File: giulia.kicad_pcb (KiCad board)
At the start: 2 copper layers, 129 parts, among them J1 AVR-ISP-6, J2 0548190519, SW1 RESET, SW2 BOOT, U1 ATmega32A-PU, Y1 16 MHz

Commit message: basic component layout
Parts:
- moved SW2 133.4 mm to (199.3, 25.8)
- moved SW1 128.5 mm to (185.2, 22.0)
- moved J1 103.9 mm to (167.1, 28.7), turned to 270 degrees
- moved C3 85.1 mm to (150.5, 53.6)
- moved C2 84.8 mm to (155.6, 31.5), turned to 180 degrees
- moved C5 72.8 mm to (150.6, 22.7)
- moved OL1 72.8 mm to (44.5, 24.0)
- moved Y1 68.2 mm to (146.3, 29.6), turned to 90 degrees
- moved J2 65.9 mm to (136.5, 30.1), turned to 270 degrees
- moved C4 65.7 mm to (150.6, 26.9)
- moved C1 62.3 mm to (125.2, 16.8), turned to 270 degrees
- moved D25 61.4 mm to (185.4, 37.0)
- moved D26 61.0 mm to (189.2, 39.5)
- moved D27 61.0 mm to (193.0, 42.0)
- moved D48 53.3 mm to (113.3, 23.2)
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
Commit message: Adjusting physical component layout
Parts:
- moved C1 15.8 mm to (117.2, 30.4)
- moved SW1 13.4 mm to (172.1, 25.0)
- moved SW2 8.69 mm to (191.4, 29.5), turned to 180 degrees
- moved J1 5.26 mm to (161.9, 29.5), turned to 90 degrees
- moved R1 3.70 mm to (98.0, 23.1)
- moved R2 3.70 mm to (98.0, 26.4)
- moved R4 3.70 mm to (98.0, 33.0)
- moved R3 3.70 mm to (98.0, 29.7)
- moved J2 2.41 mm to (136.5, 27.7)
- moved F1 2.41 mm to (127.8, 29.8)
- moved D49 1.91 mm to (113.3, 26.4)
- moved D29 0.52 mm to (200.2, 39.4)
- moved D30 0.52 mm to (204.0, 41.9)
- moved D32 0.52 mm to (211.6, 36.8)
- moved D33 0.52 mm to (215.4, 39.4)
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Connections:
- SW2 pad 1: Net-(SW2-Pad1) -> BOOT
- U1 pad 18: Net-(SW2-Pad1) -> Net-(U1-Pad18)
- U1 pad 5: Net-(U1-Pad5) -> BOOT
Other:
- board outline added: 240.9 x 112.5 mm
- board text added: "5V"
- board text added: "GND"
- board text added: "MISO"
- board text added: "MOSI"
- board text added: "RST"
- board text added: "SCK"

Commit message: PCB progress
finally placed RGB footprints, added own footprint lib for easy silkscreen adjustment etc.
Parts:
- D1, D10, D11, D12, D13, D14, D15, D16, D17, D18, D19, D2, D20, D21, D22, D23, D24, D25, D26, D27, D28, D29, D3, D30, D31, D32, D33, D34, D35, D36, D37, D38, D39, D4, D40, D41, D42, D43, D44, D45, D46, D47, D5, D6, D7, D8, D9: footprint Diode_THT:D_DO-35_SOD27_P7.62mm_Horizontal -> giulia:D_DO-35_SOD27_P7.62mm_Horizontal_Giulia
- moved D50 367.6 mm to (38.2, 31.5)
- moved D51 314.4 mm to (83.9, 31.5), turned to 180 degrees
- moved D63 289.9 mm to (50.8, 128.9)
- moved D64 283.9 mm to (33.9, 103.8), turned to 270 degrees
- moved D62 267.2 mm to (86.4, 128.9)
- moved D65 264.1 mm to (33.9, 75.7), turned to 270 degrees
- moved D61 250.9 mm to (114.9, 128.9)
- moved D52 241.1 mm to (153.0, 40.0), turned to 180 degrees
- moved D60 229.9 mm to (150.7, 128.9)
- moved D59 210.5 mm to (186.7, 128.9)
- moved D58 189.4 mm to (229.2, 128.9)
- moved D57 182.5 mm to (250.8, 128.9)
- moved D53 169.0 mm to (217.8, 31.5), turned to 180 degrees
- moved D56 147.1 mm to (267.3, 92.5), turned to 90 degrees
- moved D55 128.8 mm to (265.9, 60.3), turned to 90 degrees
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
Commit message: cleaned up libs, removed submodules
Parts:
- OL1: value OLED 128x32 -> OLED; footprint Connector_PinHeader_2.54mm:PinHeader_1x04_P2.54mm_Vertical -> giulia:OLED
- moved OL1 3.68 mm to (44.5, 27.7), turned to 270 degrees

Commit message: the madness that is trace routing begins
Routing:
- net ROW0: track 0.00 -> 237.9 mm, vias 0 -> 1
- net ROW1: track 0.00 -> 233.1 mm, vias 0 -> 1
- net ROW3: track 0.00 -> 232.7 mm
- net ROW2: track 0.00 -> 231.6 mm, vias 0 -> 1
- net +5V: track 0.00 -> 164.4 mm, vias 0 -> 1
- net GND: track 0.00 -> 128.6 mm
- net Net-(D50-Pad4): track 0.00 -> 58.1 mm
- net D+: track 0.00 -> 44.6 mm
- net D-: track 0.00 -> 41.6 mm
- net Net-(D48-Pad1): track 0.00 -> 40.2 mm
- net Net-(D49-Pad1): track 0.00 -> 31.1 mm
- net BOOT: track 0.00 -> 26.7 mm
- net RST: track 0.00 -> 24.1 mm
- net RGB: track 0.00 -> 21.5 mm
- net Net-(C5-Pad1): track 0.00 -> 16.6 mm
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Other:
- net class Default: trace_width 0.25 -> 0.254
- net class Power added: clearance 0.2, trace_width 0.381, via_dia 0.8, via_drill 0.4

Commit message: top layout that makes more sense
imagine that, not using 20 vias for basic USB wiring
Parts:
- moved J2 41.9 mm to (94.6, 27.7)
- moved R2 33.7 mm to (131.7, 25.7), turned to 180 degrees
- moved R3 33.7 mm to (131.7, 29.0), turned to 180 degrees
- moved F1 29.8 mm to (98.2, 33.4), turned to 180 degrees
- moved R1 23.5 mm to (121.5, 22.4)
- moved R4 23.5 mm to (121.5, 32.3)
- moved D58 14.0 mm to (215.3, 128.9)
- moved D48 12.2 mm to (101.6, 26.5)
- moved D49 12.1 mm to (101.6, 23.2)
- moved C1 8.56 mm to (109.2, 33.4), turned to 90 degrees
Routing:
- net COL0: track 0.00 -> 160.4 mm
- net COL1: track 0.00 -> 146.9 mm
- net COL11: track 0.00 -> 137.7 mm
- net COL2: track 0.00 -> 130.4 mm
- net COL10: track 0.00 -> 118.4 mm
- net COL3: track 0.00 -> 113.9 mm
- net COL4: track 0.00 -> 109.8 mm
- net COL9: track 0.00 -> 101.9 mm
- net COL5: track 0.00 -> 92.7 mm
- net COL8: track 0.00 -> 85.4 mm
- net +5V: track 164.4 -> 83.9 mm, vias 1 -> 0
- net COL7: track 0.00 -> 71.2 mm
- net Net-(D50-Pad4): track 58.1 -> 0.00 mm
- net COL6: track 0.00 -> 56.1 mm
- net RST: track 24.1 -> 68.0 mm
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
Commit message: routing progress, diode placement change
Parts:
- moved D16 11.5 mm to (78.7, 38.0)
- moved D24 11.5 mm to (109.2, 38.0)
- moved D8 11.5 mm to (48.3, 38.0)
- moved D13 11.4 mm to (90.2, 44.1)
- moved D21 11.4 mm to (120.7, 44.1)
- moved D5 11.4 mm to (59.7, 44.1)
- moved D15 3.84 mm to (82.5, 40.0)
- moved D23 3.84 mm to (113.0, 40.0)
- moved D7 3.84 mm to (52.1, 40.0)
- moved D14 3.81 mm to (86.4, 42.0)
- moved D22 3.81 mm to (116.8, 42.0)
- moved D6 3.81 mm to (55.9, 42.0)
- moved D12 1.02 mm to (74.9, 38.0)
- moved D20 1.02 mm to (105.4, 38.0)
- moved D4 1.02 mm to (44.5, 38.0)
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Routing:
- net ROW3: track 232.7 -> 119.4 mm
- net ROW2: track 231.6 -> 123.2 mm, vias 1 -> 0
- net ROW0: track 237.9 -> 130.8 mm, vias 1 -> 0
- net ROW1: track 233.1 -> 127.0 mm, vias 1 -> 0
- net Net-(D20-Pad2): track 0.00 -> 95.5 mm
- net Net-(D24-Pad2): track 0.00 -> 94.0 mm
- net Net-(D12-Pad2): track 0.00 -> 90.4 mm
- net Net-(D4-Pad2): track 0.00 -> 81.4 mm
- net Net-(D16-Pad2): track 0.00 -> 81.3 mm
- net Net-(D8-Pad2): track 0.00 -> 78.9 mm
- net Net-(D19-Pad2): track 0.00 -> 77.2 mm
- net Net-(D23-Pad2): track 0.00 -> 68.6 mm
- net Net-(D15-Pad2): track 0.00 -> 62.9 mm
- net Net-(D11-Pad2): track 0.00 -> 62.7 mm
- net Net-(D7-Pad2): track 0.00 -> 61.0 mm
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
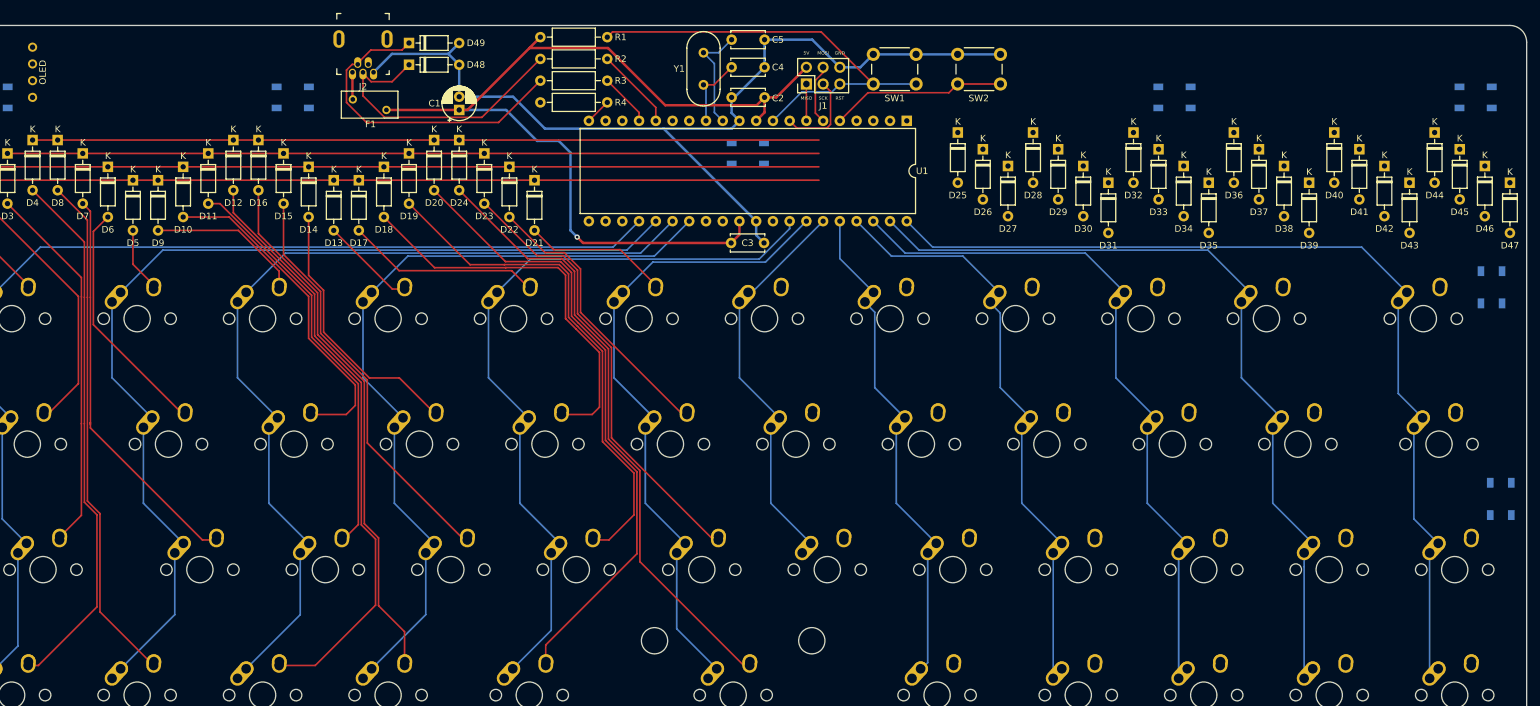
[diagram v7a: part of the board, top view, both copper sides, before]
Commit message: switch routing done, fixed MCU position
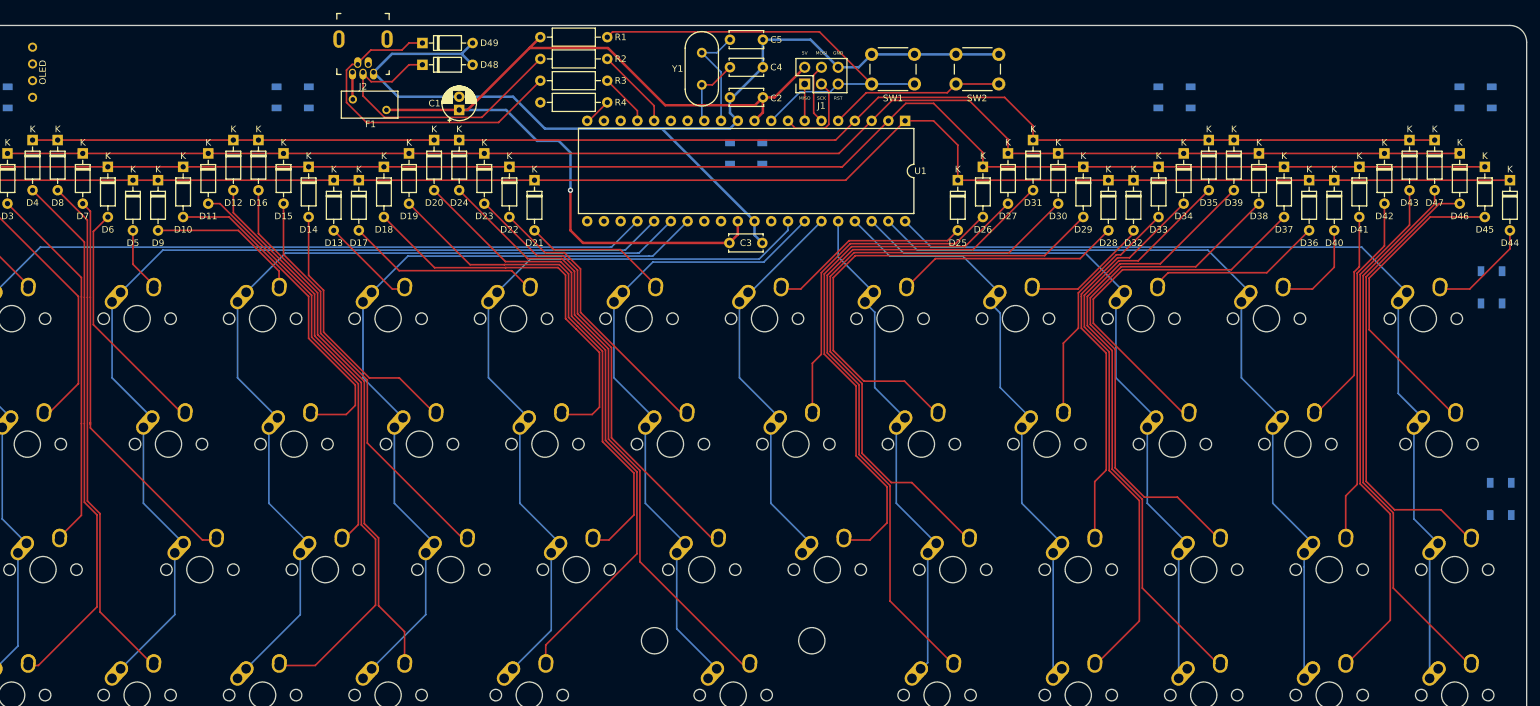
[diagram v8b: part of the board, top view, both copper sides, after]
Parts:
- moved D36 13.5 mm to (238.3, 44.1)
- moved D44 13.5 mm to (268.7, 44.1)
- moved D28 13.5 mm to (207.8, 44.1)
- moved D39 13.1 mm to (226.8, 38.0)
- moved D47 13.1 mm to (257.3, 38.0)
- moved D31 13.1 mm to (196.3, 38.0)
- moved D25 7.24 mm to (184.9, 44.1)
- moved D32 7.24 mm to (211.6, 44.1)
- moved D40 7.24 mm to (242.1, 44.1)
- moved D35 6.48 mm to (223.0, 38.0)
- moved D43 6.48 mm to (253.5, 38.0)
- moved D29 4.65 mm to (204.0, 42.0)
- moved D37 4.65 mm to (234.4, 42.0)
- moved D45 4.65 mm to (264.9, 42.0)
- moved D30 4.26 mm to (200.2, 40.0)
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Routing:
- net ROW0: track 130.8 -> 246.3 mm
- net ROW1: track 127.0 -> 237.3 mm
- net ROW2: track 123.2 -> 228.4 mm
- net Net-(D31-Pad2): track 0.00 -> 103.9 mm
- net ROW3: track 119.4 -> 219.5 mm
- net Net-(D39-Pad2): track 0.00 -> 93.3 mm
- net Net-(D30-Pad2): track 0.00 -> 89.8 mm
- net Net-(D35-Pad2): track 0.00 -> 88.0 mm
- net Net-(D47-Pad2): track 0.00 -> 83.5 mm
- net Net-(D27-Pad2): track 0.00 -> 81.7 mm
- net Net-(D43-Pad2): track 0.00 -> 79.9 mm
- net Net-(D38-Pad2): track 0.00 -> 79.4 mm
- net Net-(D29-Pad2): track 0.00 -> 72.7 mm
- net Net-(D46-Pad2): track 0.00 -> 69.5 mm
- net Net-(D34-Pad2): track 0.00 -> 60.8 mm
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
